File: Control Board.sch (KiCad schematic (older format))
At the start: 29 parts, among them P1 CONN_01X12, P10 CONN_01X12, P2 CONN_01X12, P3 CONN_01X12, P4 CONN_01X12, P5 CONN_01X05, P6 CONN_01X12, P7 CONN_01X12, P8 CONN_01X05, P9 CONN_01X12, U1 MMA8451Q, U2 MMA8451Q, U3 MMA8451Q, U4 RLOOP_NODE_CORE

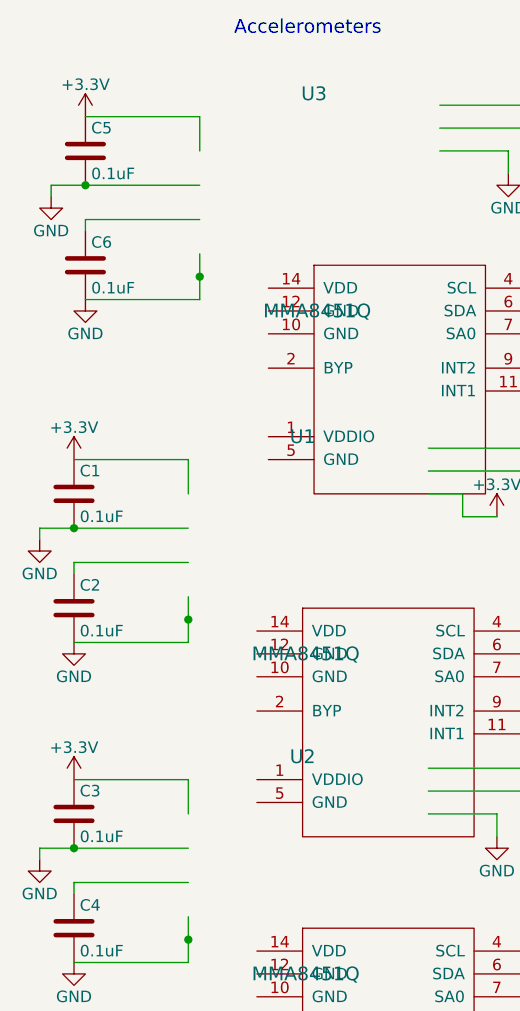
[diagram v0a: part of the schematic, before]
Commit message: Update Control Board.sch
Sean's most recent version, mostly complete, possibly a few more changes necessary
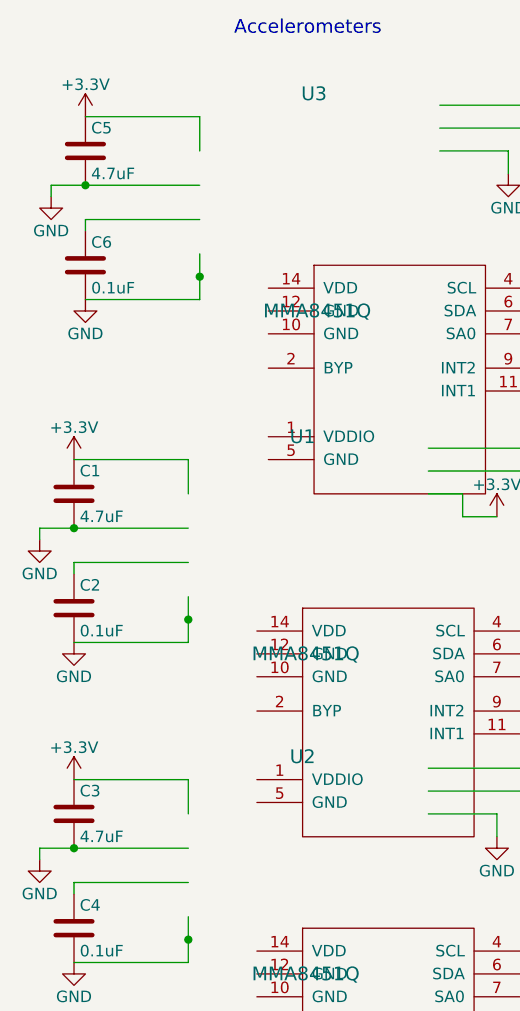
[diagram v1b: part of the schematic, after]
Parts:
- C1, C3, C5: value 0.1uF -> 4.7uF
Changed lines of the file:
@@
 LIBS:contrib
 LIBS:valves
-LIBS:rloop
 LIBS:Control Board-cache
 EELAYER 25 0
@@
 P 1000 1800
 F 0 "C5" H 1025 1900 50  0000 L CNN
-F 1 "0.1uF" H 1025 1700 50  0000 L CNN
+F 1 "4.7uF" H 1025 1700 50  0000 L CNN
 F 2 "" H 1038 1650 50  0000 C CNN
 F 3 "" H 1000 1800 50  0000 C CNN
@@
 P 950 3300
 F 0 "C1" H 975 3400 50  0000 L CNN
-F 1 "0.1uF" H 975 3200 50  0000 L CNN
+F 1 "4.7uF" H 975 3200 50  0000 L CNN
 F 2 "" H 988 3150 50  0000 C CNN
 F 3 "" H 950 3300 50  0000 C CNN
@@
 P 950 4700
 F 0 "C3" H 975 4800 50  0000 L CNN
-F 1 "0.1uF" H 975 4600 50  0000 L CNN
+F 1 "4.7uF" H 975 4600 50  0000 L CNN
 F 2 "" H 988 4550 50  0000 C CNN
 F 3 "" H 950 4700 50  0000 C CNN

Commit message: Update Control Board.sch
Added test point on trigger input & changed VDD cap val (0.1uF --> 4.7uF)
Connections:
- net labels added: P1
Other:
- note added: "Test Point\n"
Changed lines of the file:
@@
 	4000 6200 4650 6200
 Wire Wire Line
-	4000 6100 4650 6100
+	4000 6100 5150 6100
 Text Label 4300 6500 0    60   ~ 0
 LRF_Tx
@@
 	5250 4500 5250 4350
 Connection ~ 5150 4500
+Text Label 5150 6100 0    60   ~ 0
+P1
+Connection ~ 4650 6100
+Text Notes 5350 6100 0    60   ~ 0
+Test Point\n
 $EndSCHEMATC

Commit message: update
2nd test point added
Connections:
- net labels added: P2
- wire segments 140 -> 158
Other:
- note added: "Test Point x2\n"
- note removed: "Test Point\n"
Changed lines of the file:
@@
 	1500 2450 1000 2450
 Wire Wire Line
-	1450 3750 1450 3950
+	1450 3750 1450 3850
+Wire Wire Line
+	1450 3850 1450 3950
 Connection ~ 1450 3850
 Wire Wire Line
@@
 	1000 2100 1000 2150
 Wire Wire Line
-	850  1950 1500 1950
+	850  1950 1000 1950
+Wire Wire Line
+	1000 1950 1500 1950
 Wire Wire Line
 	850  1950 850  2000
@@
 	950  3600 950  3650
 Wire Wire Line
-	800  3450 1450 3450
+	800  3450 950  3450
+Wire Wire Line
+	950  3450 1450 3450
 Wire Wire Line
 	800  3450 800  3500
@@
 	950  5000 950  5050
 Wire Wire Line
-	800  4850 1450 4850
+	800  4850 950  4850
+Wire Wire Line
+	950  4850 1450 4850
 Wire Wire Line
 	800  4850 800  4900
@@
 	1500 1650 1500 1800
 Wire Wire Line
-	1500 2250 1500 2450
+	1500 2250 1500 2350
+Wire Wire Line
+	1500 2350 1500 2450
 Connection ~ 1500 2350
 Wire Wire Line
 	1450 4700 1450 4550
 Wire Wire Line
-	1450 5150 1450 5350
+	1450 5150 1450 5250
+Wire Wire Line
+	1450 5250 1450 5350
 Connection ~ 1450 5250
 Wire Wire Line
@@
 	2550 1600 3550 1600
 Wire Wire Line
-	3550 1600 3550 3100
+	3550 1600 3550 2750
+Wire Wire Line
+	3550 2750 3550 3100
 Wire Wire Line
 	3550 2750 4400 2750
@@
 	2550 1700 3300 1700
 Wire Wire Line
-	3300 1700 3300 3200
+	3300 1700 3300 2650
+Wire Wire Line
+	3300 2650 3300 3200
 Wire Wire Line
 	3300 3200 2500 3200
@@
 	5050 4350 5050 4500
 Wire Wire Line
-	5050 4500 5250 4500
+	5050 4500 5150 4500
+Wire Wire Line
+	5150 4500 5250 4500
 Wire Wire Line
 	5150 4500 5150 4350
@@
 	5300 900  5200 900
 Wire Wire Line
-	10300 1700 10600 1700
+	10300 1700 10450 1700
+Wire Wire Line
+	10450 1700 10600 1700
 Wire Wire Line
 	10600 1700 10600 1950
@@
 	9600 1550 9850 1550
 Wire Wire Line
-	9450 1700 9750 1700
+	9450 1700 9600 1700
+Wire Wire Line
+	9600 1700 9750 1700
 Wire Wire Line
 	9750 1700 9750 1950
@@
 	10450 3250 10700 3250
 Wire Wire Line
-	10300 3400 10600 3400
+	10300 3400 10450 3400
+Wire Wire Line
+	10450 3400 10600 3400
 Wire Wire Line
 	10600 3400 10600 3650
@@
 	9600 3250 9850 3250
 Wire Wire Line
-	9450 3400 9750 3400
+	9450 3400 9600 3400
+Wire Wire Line
+	9600 3400 9750 3400
 Wire Wire Line
 	9750 3400 9750 3650
@@
 	8650 1550 8900 1550
 Wire Wire Line
-	8500 1700 8800 1700
+	8500 1700 8650 1700
+Wire Wire Line
+	8650 1700 8800 1700
 Wire Wire Line
 	8800 1700 8800 1950
@@
 	7800 1550 8050 1550
 Wire Wire Line
-	7650 1700 7950 1700
+	7650 1700 7800 1700
+Wire Wire Line
+	7800 1700 7950 1700
 Wire Wire Line
 	7950 1700 7950 1950
@@
 	8650 3250 8900 3250
 Wire Wire Line
-	8500 3400 8800 3400
+	8500 3400 8650 3400
+Wire Wire Line
+	8650 3400 8800 3400
 Wire Wire Line
 	8800 3400 8800 3650
@@
 	7800 3250 8050 3250
 Wire Wire Line
-	7650 3400 7950 3400
+	7650 3400 7800 3400
+Wire Wire Line
+	7800 3400 7950 3400
 Wire Wire Line
 	7950 3400 7950 3650
@@
 	4000 6300 4650 6300
 Wire Wire Line
+	4650 6300 5150 6300
+Wire Wire Line
 	4000 6200 4650 6200
 Wire Wire Line
-	4000 6100 5150 6100
+	4650 6200 5150 6200
 Text Label 4300 6500 0    60   ~ 0
 LRF_Tx
@@
 	5250 4500 5250 4350
 Connection ~ 5150 4500
-Text Label 5150 6100 0    60   ~ 0
+Text Notes 5400 6250 0    60   ~ 0
+Test Point x2\n
+Connection ~ 4650 6200
+Connection ~ 4650 6300
+Text Label 5150 6200 0    60   ~ 0
 P1
-Connection ~ 4650 6100
-Text Notes 5350 6100 0    60   ~ 0
-Test Point\n
+Text Label 5150 6300 0    60   ~ 0
+P2
 $EndSCHEMATC

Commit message: Split laser interface to new sheet.
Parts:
- removed P?: CONN_01X07, symbol CONN_01X07
- U1, U2, U3: symbol MMA8451Q -> MMA8451Q-RESCUE-Control_Board
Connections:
- net labels removed: LRD_Analog_Output, LRD_Trigger_Input, LRF_Trigger_Output, P1, P2
- wire segments 158 -> 131
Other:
- note added: "rLoop - Control Node"
- note removed: "Laser Rangefinder CM3-30\nRS-232"
- note removed: "Test Point x2\n"
- moved on the sheet: U1, U2, U3
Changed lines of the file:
@@
 EESchema Schematic File Version 2
+LIBS:Control Board-rescue
 LIBS:power
 LIBS:device
@@
 LIBS:contrib
 LIBS:valves
+LIBS:rloop
 LIBS:Control Board-cache
 EELAYER 25 0
 EELAYER END
-$Descr A4 11693 8268
+$Descr A3 16535 11693
 encoding utf-8
-Sheet 1 1
-Title ""
+Sheet 1 2
+Title "Control Node - Overview"
 Date ""
-Rev ""
+Rev "1"
 Comp ""
 Comment1 ""
@@
 $EndDescr
 $Comp
-L MMA8451Q U1
+L MMA8451Q-RESCUE-Control_Board U1
 U 1 1 571E86E7
 P 1950 3800
@@
 $EndComp
 $Comp
-L MMA8451Q U2
+L MMA8451Q-RESCUE-Control_Board U2
 U 1 1 571E8774
 P 1950 5200
@@
 $EndComp
 $Comp
-L MMA8451Q U3
+L MMA8451Q-RESCUE-Control_Board U3
 U 1 1 571E8799
 P 2000 2300
@@
 Text Notes 1650 1300 0    60   ~ 0
 Accelerometers
-$Comp
-L CONN_01X07 P?
-U 1 1 5721A0BE
-P 3800 6400
-F 0 "P?" H 3800 6800 50  0000 C CNN
-F 1 "CONN_01X07" V 3900 6400 50  0000 C CNN
-F 2 "" H 3800 6400 50  0000 C CNN
-F 3 "" H 3800 6400 50  0000 C CNN
-	1    3800 6400
-	-1   0    0    1
-$EndComp
-Text Notes 3400 5950 0    60   ~ 0
-Laser Rangefinder CM3-30\nRS-232
-$Comp
-L +24V #PWR?
-U 1 1 5721A87F
-P 4400 7000
-F 0 "#PWR?" H 4400 6850 50  0001 C CNN
-F 1 "+24V" H 4400 7140 50  0000 C CNN
-F 2 "" H 4400 7000 50  0000 C CNN
-F 3 "" H 4400 7000 50  0000 C CNN
-	1    4400 7000
-	1    0    0    -1
-$EndComp
-$Comp
-L GND #PWR?
-U 1 1 5721ADC5
-P 4650 6750
-F 0 "#PWR?" H 4650 6500 50  0001 C CNN
-F 1 "GND" H 4650 6600 50  0000 C CNN
-F 2 "" H 4650 6750 50  0000 C CNN
-F 3 "" H 4650 6750 50  0000 C CNN
-	1    4650 6750
-	1    0    0    -1
-$EndComp
 Wire Wire Line
 	1450 3300 1450 3150
@@
 	1500 2450 1000 2450
 Wire Wire Line
-	1450 3750 1450 3850
-Wire Wire Line
-	1450 3850 1450 3950
+	1450 3750 1450 3950
 Connection ~ 1450 3850
 Wire Wire Line
@@
 	1000 2100 1000 2150
 Wire Wire Line
-	850  1950 1000 1950
-Wire Wire Line
-	1000 1950 1500 1950
+	850  1950 1500 1950
 Wire Wire Line
 	850  1950 850  2000
@@
 	950  3600 950  3650
 Wire Wire Line
-	800  3450 950  3450
-Wire Wire Line
-	950  3450 1450 3450
+	800  3450 1450 3450
 Wire Wire Line
 	800  3450 800  3500
@@
 	950  5000 950  5050
 Wire Wire Line
-	800  4850 950  4850
-Wire Wire Line
-	950  4850 1450 4850
+	800  4850 1450 4850
 Wire Wire Line
 	800  4850 800  4900
@@
 	1500 1650 1500 1800
 Wire Wire Line
-	1500 2250 1500 2350
-Wire Wire Line
-	1500 2350 1500 2450
+	1500 2250 1500 2450
 Connection ~ 1500 2350
 Wire Wire Line
 	1450 4700 1450 4550
 Wire Wire Line
-	1450 5150 1450 5250
-Wire Wire Line
-	1450 5250 1450 5350
+	1450 5150 1450 5350
 Connection ~ 1450 5250
 Wire Wire Line
@@
 	2550 1600 3550 1600
 Wire Wire Line
-	3550 1600 3550 2750
-Wire Wire Line
-	3550 2750 3550 3100
+	3550 1600 3550 3100
 Wire Wire Line
 	3550 2750 4400 2750
@@
 	2550 1700 3300 1700
 Wire Wire Line
-	3300 1700 3300 2650
-Wire Wire Line
-	3300 2650 3300 3200
+	3300 1700 3300 3200
 Wire Wire Line
 	3300 3200 2500 3200
@@
 	5050 4350 5050 4500
 Wire Wire Line
-	5050 4500 5150 4500
-Wire Wire Line
-	5150 4500 5250 4500
+	5050 4500 5250 4500
 Wire Wire Line
 	5150 4500 5150 4350
@@
 	5300 900  5200 900
 Wire Wire Line
-	10300 1700 10450 1700
-Wire Wire Line
-	10450 1700 10600 1700
+	10300 1700 10600 1700
 Wire Wire Line
 	10600 1700 10600 1950
@@
 	9600 1550 9850 1550
 Wire Wire Line
-	9450 1700 9600 1700
-Wire Wire Line
-	9600 1700 9750 1700
+	9450 1700 9750 1700
 Wire Wire Line
 	9750 1700 9750 1950
@@
 	10450 3250 10700 3250
 Wire Wire Line
-	10300 3400 10450 3400
-Wire Wire Line
-	10450 3400 10600 3400
+	10300 3400 10600 3400
 Wire Wire Line
 	10600 3400 10600 3650
@@
 	9600 3250 9850 3250
 Wire Wire Line
-	9450 3400 9600 3400
-Wire Wire Line
-	9600 3400 9750 3400
+	9450 3400 9750 3400
 Wire Wire Line
 	9750 3400 9750 3650
@@
 	8650 1550 8900 1550
 Wire Wire Line
-	8500 1700 8650 1700
-Wire Wire Line
-	8650 1700 8800 1700
+	8500 1700 8800 1700
 Wire Wire Line
 	8800 1700 8800 1950
@@
 	7800 1550 8050 1550
 Wire Wire Line
-	7650 1700 7800 1700
-Wire Wire Line
-	7800 1700 7950 1700
+	7650 1700 7950 1700
 Wire Wire Line
 	7950 1700 7950 1950
@@
 	8650 3250 8900 3250
 Wire Wire Line
-	8500 3400 8650 3400
-Wire Wire Line
-	8650 3400 8800 3400
+	8500 3400 8800 3400
 Wire Wire Line
 	8800 3400 8800 3650
@@
 	7800 3250 8050 3250
 Wire Wire Line
-	7650 3400 7800 3400
-Wire Wire Line
-	7800 3400 7950 3400
+	7650 3400 7950 3400
 Wire Wire Line
 	7950 3400 7950 3650
@@
 Wire Wire Line
 	3700 2950 3700 4500
-Wire Wire Line
-	4000 6700 4000 7000
-Wire Wire Line
-	4000 7000 4400 7000
-Wire Wire Line
-	4000 6600 4650 6600
-Wire Wire Line
-	4650 6600 4650 6750
-Wire Wire Line
-	4000 6500 4650 6500
-Wire Wire Line
-	4000 6400 4650 6400
-Wire Wire Line
-	4000 6300 4650 6300
-Wire Wire Line
-	4650 6300 5150 6300
-Wire Wire Line
-	4000 6200 4650 6200
-Wire Wire Line
-	4650 6200 5150 6200
-Text Label 4300 6500 0    60   ~ 0
-LRF_Tx
-Text Label 4300 6400 0    60   ~ 0
-LRF_Rx
-Text Label 4100 6300 0    60   ~ 0
-LRF_Trigger_Output
-Text Label 4100 6200 0    60   ~ 0
-LRD_Analog_Output
-Text Label 4100 6100 0    60   ~ 0
-LRD_Trigger_Input
 Wire Wire Line
 	4400 3150 4200 3150
@@
 	5250 4500 5250 4350
 Connection ~ 5150 4500
-Text Notes 5400 6250 0    60   ~ 0
-Test Point x2\n
-Connection ~ 4650 6200
-Connection ~ 4650 6300
-Text Label 5150 6200 0    60   ~ 0
-P1
-Text Label 5150 6300 0    60   ~ 0
-P2
+Text Notes 11950 10200 0    118  ~ 0
+rLoop - Control Node
+$Sheet
+S 1700 8650 1500 1200
+U 5753FE7B
+F0 "Sheet_Laser" 118
+F1 "ControlNode_Laser.sch" 118
+F2 "LASER_RX" O R 3200 8750 63
+F3 "LASER_TX" I R 3200 8850 63
+$EndSheet
 $EndSCHEMATC

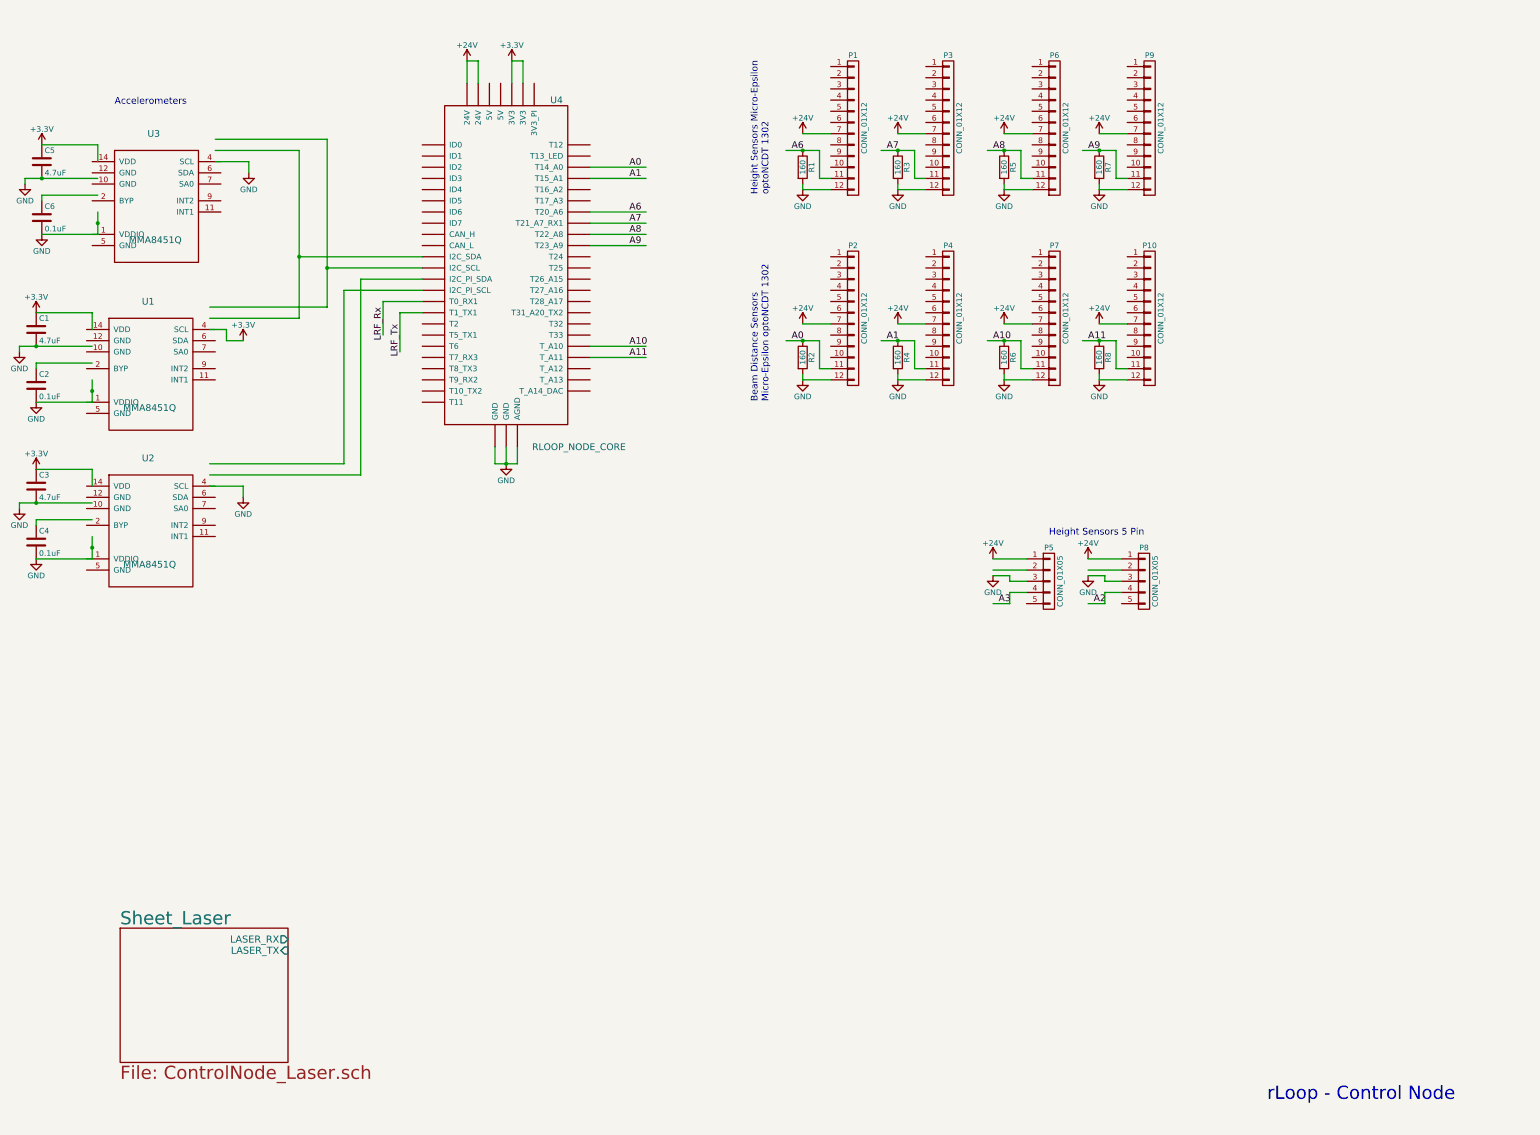
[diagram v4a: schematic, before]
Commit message: Split accels off to separate sheet.
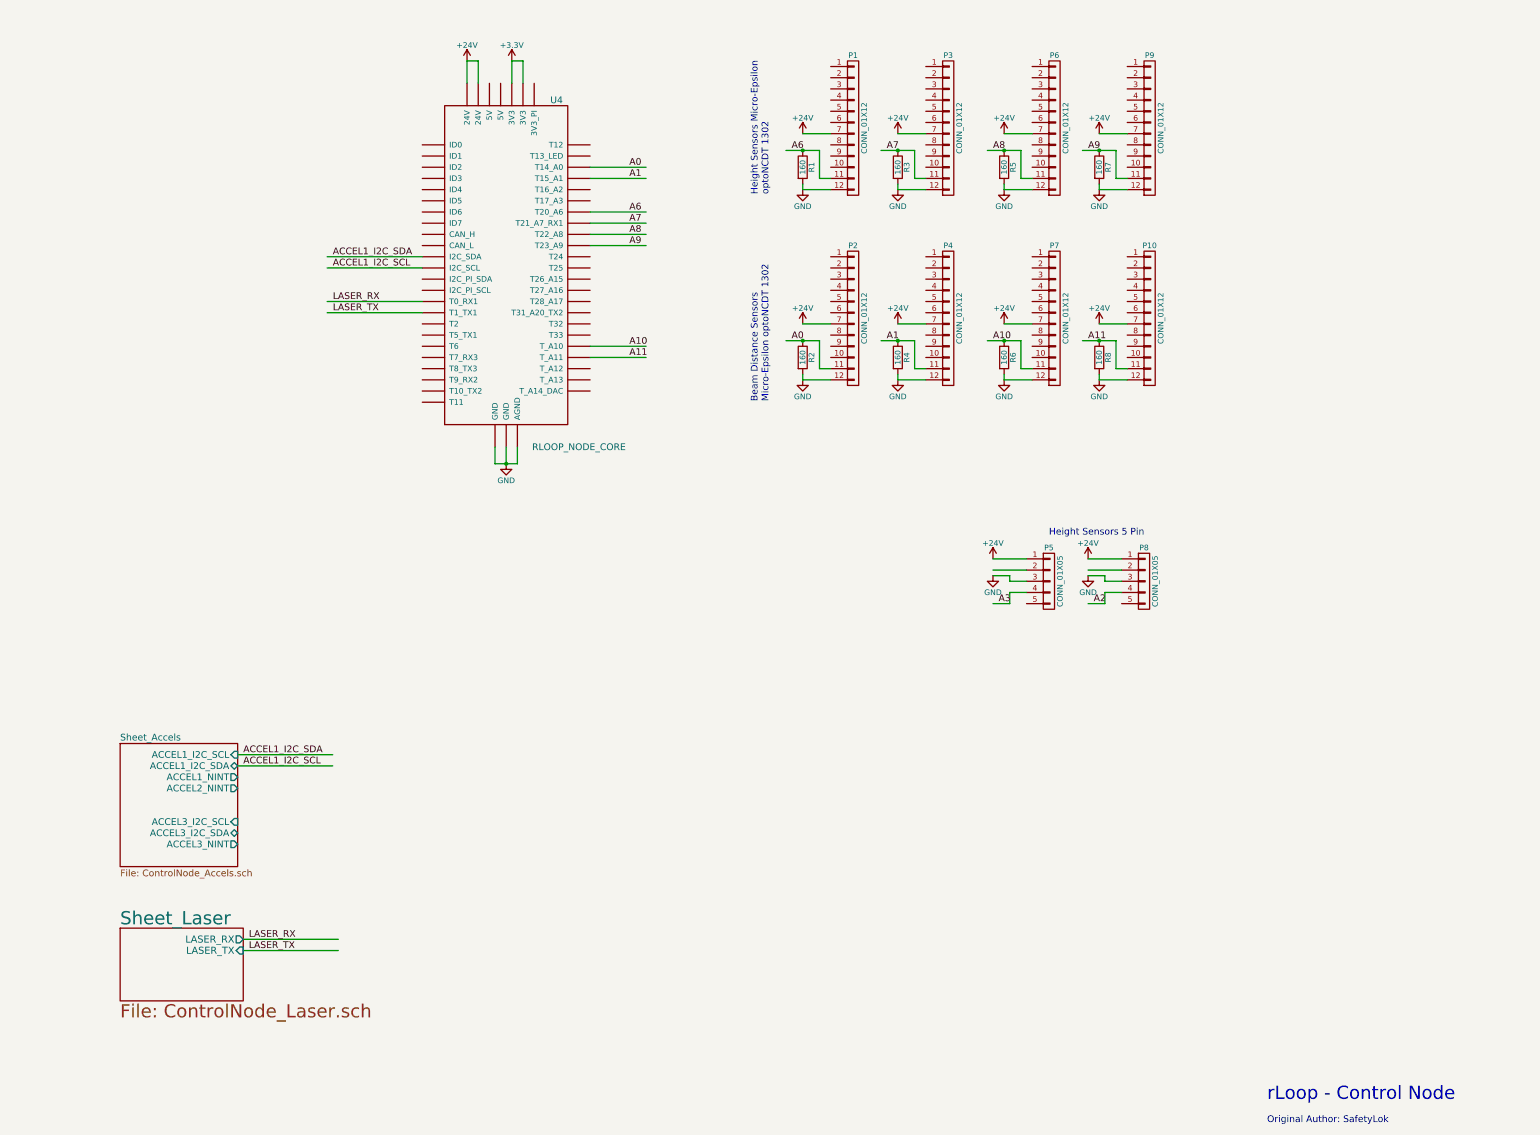
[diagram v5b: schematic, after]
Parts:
- removed C1, C3, C5: 4.7uF, symbol C
- removed C2, C4, C6: 0.1uF, symbol C
- removed U1, U2, U3: MMA8451Q, symbol MMA8451Q-RESCUE-Control_Board
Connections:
- net labels added: ACCEL1_I2C_SCL, ACCEL1_I2C_SDA, LASER_RX, LASER_TX
- net labels removed: LRF_Rx, LRF_Tx
- wire segments 131 -> 90
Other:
- note added: "Original Author: SafetyLok"
- note removed: "Accelerometers"
